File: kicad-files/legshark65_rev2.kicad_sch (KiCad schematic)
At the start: 203 parts, among them J1 ARM JTAG, SW1 K2-1187SQ-A4SW-06, SW2 PCM12SMTR, T2 53261-0471, U1 STM32F411CEU6, U2 MCP1700T-3302E/TT, U3 AT24C256C-SSHL-T, Y1 TAXM8M4RFDCET2T

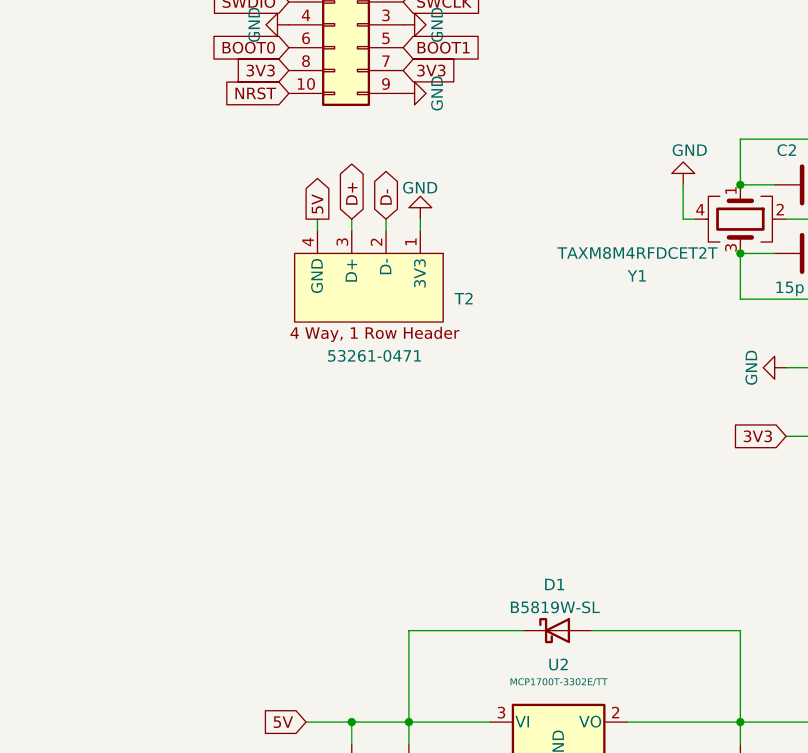
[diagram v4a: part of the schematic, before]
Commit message: Added EZMate connector and optional JST pads
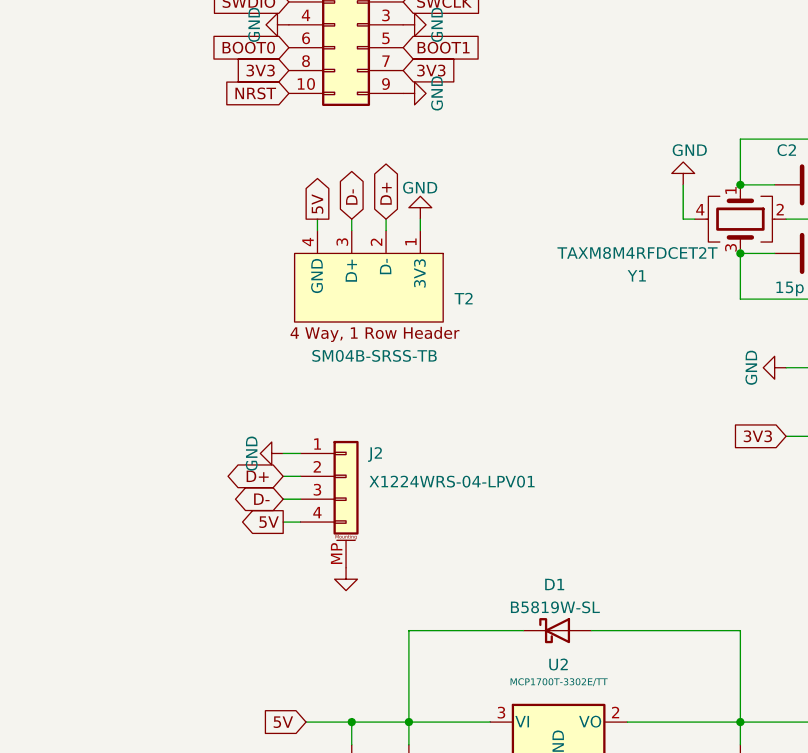
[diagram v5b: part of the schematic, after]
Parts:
- added J2: X1224WRS-04-LPV01, Legshark:PicoEZMate-Reinforced-Alt, symbol Connector_Generic_MountingPin:Conn_01x04_MountingPin
- T2: value 53261-0471 -> SM04B-SRSS-TB; footprint Legshark:Molex, PicoBlade, 53261, 4 Way, 1 Row, Right Angle PCB Header -> acheron_Connectors:SM04B-SRSS-TB(LF)(SN)
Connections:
- net 5V: now also J2.4 (Pin_4)
- net D+: now also T2.2 (D-), J2.2 (Pin_2); no longer T2.3 (D+)
- net D-: now also T2.3 (D+), J2.3 (Pin_3); no longer T2.2 (D-)
- net GND: now also J2.1 (Pin_1), J2.MP (MountPin)
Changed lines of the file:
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@@
     (stroke (width 0) (type default))
   )
+  (wire (pts (xy 41.91 266.065) (xy 43.815 266.065))
+    (stroke (width 0) (type default))
+  )
   (wire (pts (xy 325.12 16.51) (xy 325.12 24.13))
     (stroke (width 0) (type default))
@@
     (stroke (width 0) (type default))
   )
+  (wire (pts (xy 41.91 258.445) (xy 43.815 258.445))
+    (stroke (width 0) (type default))
+  )
   (wire (pts (xy 119.38 248.92) (xy 125.73 248.92))
     (stroke (width 0) (type default))
@@
     (stroke (width 0) (type default))
   )
+  (wire (pts (xy 43.815 260.985) (xy 41.91 260.985))
+    (stroke (width 0) (type default))
+  )
   (wire (pts (xy 91.44 158.75) (xy 96.52 158.75))
     (stroke (width 0) (type default))
@@
     (stroke (width 0) (type default))
   )
+  (wire (pts (xy 41.91 263.525) (xy 43.815 263.525))
+    (stroke (width 0) (type default))
+  )
   (wire (pts (xy 238.125 123.19) (xy 242.57 123.19))
     (stroke (width 0) (type default))
@@
     )
   )
-  (global_label "D-" (shape bidirectional) (at 53.34 232.41 90) (fields_autoplaced)
+  (global_label "5V" (shape output) (at 41.91 266.065 180) (fields_autoplaced)
+    (effects (font (size 1.27 1.27)) (justify right))
+    (property "Intersheetrefs" "${INTERSHEET_REFS}" (at 37.3603 266.065 0)
+      (effects (font (size 1.27 1.27)) (justify right) hide)
+    )
+  )
+  (global_label "D-" (shape bidirectional) (at 49.53 232.41 90) (fields_autoplaced)
     (effects (font (size 1.27 1.27)) (justify left))
-    (property "Intersheetrefs" "${INTERSHEET_REFS}" (at 53.34 226.3635 90)
+    (property "Intersheetrefs" "${INTERSHEET_REFS}" (at 49.53 226.3635 90)
       (effects (font (size 1.27 1.27)) (justify left) hide)
     )
@@
     )
   )
+  (global_label "D-" (shape bidirectional) (at 41.91 263.525 180) (fields_autoplaced)
+    (effects (font (size 1.27 1.27)) (justify right))
+    (property "Intersheetrefs" "${INTERSHEET_REFS}" (at 35.8635 263.525 0)
+      (effects (font (size 1.27 1.27)) (justify right) hide)
+    )
+  )
   (global_label "3V3" (shape input) (at 125.73 201.295 90) (fields_autoplaced)
     (effects (font (size 1.27 1.27)) (justify left))
@@
     )
   )
+  (global_label "D+" (shape bidirectional) (at 41.91 260.985 180) (fields_autoplaced)
+    (effects (font (size 1.27 1.27)) (justify right))
+    (property "Intersheetrefs" "${INTERSHEET_REFS}" (at 35.8635 260.985 0)
+      (effects (font (size 1.27 1.27)) (justify right) hide)
+    )
+  )
   (global_label "row4" (shape input) (at 125.73 223.52 180)
     (effects (font (size 1.27 1.27)) (justify right))
@@
     )
   )
-  (global_label "D+" (shape bidirectional) (at 49.53 232.41 90) (fields_autoplaced)
+  (global_label "D+" (shape bidirectional) (at 53.34 232.41 90) (fields_autoplaced)
     (effects (font (size 1.27 1.27)) (justify left))
-    (property "Intersheetrefs" "${INTERSHEET_REFS}" (at 49.53 226.3635 90)
+    (property "Intersheetrefs" "${INTERSHEET_REFS}" (at 53.34 226.3635 90)
       (effects (font (size 1.27 1.27)) (justify left) hide)
     )
@@
     )
   )
+  (symbol (lib_id "Connector_Generic_MountingPin:Conn_01x04_MountingPin") (at 48.895 260.985 0) (unit 1)
+    (in_bom yes) (on_board yes) (dnp no)
+    (property "Reference" "J2" (at 51.435 258.445 0)
+      (effects (font (size 1.27 1.27)) (justify left))
+    )
+    (property "Value" "X1224WRS-04-LPV01" (at 51.435 261.62 0)
+      (effects (font (size 1.27 1.27)) (justify left))
+    )
+    (property "Footprint" "Legshark:PicoEZMate-Reinforced-Alt" (at 48.895 260.985 0)
+      (effects (font (size 1.27 1.27)) hide)
+    )
+    (property "Datasheet" "~" (at 48.895 260.985 0)
+      (effects (font (size 1.27 1.27)) hide)
+    )
+    (property "Manufacturer" "XKB Connectivity" (at 48.895 260.985 0)
+      (effects (font (size 1.27 1.27)) hide)
+    )
+    (property "Manufacturer Part Number" "X1224WRS-04-LPV01" (at 48.895 260.985 0)
+      (effects (font (size 1.27 1.27)) hide)
+    )
+    (property "LCSC Part Number" "C528030" (at 48.895 260.985 0)
+      (effects (font (size 1.27 1.27)) hide)
+    )
+    (pin "1")
+    (pin "2")
+    (pin "3")
+    (pin "4")
+    (pin "MP")
+    (instances
+      (project "legshark65_rev2"
+        (path "/2fcc1073-d3f4-43f9-b3b4-5cee13272705"
+          (reference "J2") (unit 1)
+        )
+      )
+      (project "UDB"
+        (path "/c4c12ac1-bf97-4e49-b99b-b461a52b064e"
+          (reference "J2") (unit 1)
+        )
+      )
+    )
+  )
   (symbol (lib_id "Mechanical:MountingHole") (at 243.84 174.625 0) (unit 1)
     (in_bom yes) (on_board yes) (dnp no) (fields_autoplaced)
@@
     )
   )
+  (symbol (lib_id "power:GND") (at 48.895 271.145 0) (unit 1)
+    (in_bom yes) (on_board yes) (dnp no)
+    (property "Reference" "#PWR037" (at 48.895 277.495 0)
+      (effects (font (size 1.27 1.27)) hide)
+    )
+    (property "Value" "GND" (at 49.022 275.5392 0)
+      (effects (font (size 1.27 1.27)) hide)
+    )
+    (property "Footprint" "" (at 48.895 271.145 0)
+      (effects (font (size 1.27 1.27)) hide)
+    )
+    (property "Datasheet" "" (at 48.895 271.145 0)
+      (effects (font (size 1.27 1.27)) hide)
+    )
+    (pin "1")
+    (instances
+      (project "legshark65_rev2"
+        (path "/2fcc1073-d3f4-43f9-b3b4-5cee13272705"
+          (reference "#PWR037") (unit 1)
+        )
+      )
+      (project "UDB"
+        (path "/c4c12ac1-bf97-4e49-b99b-b461a52b064e"
+          (reference "#PWR011") (unit 1)
+        )
+      )
+    )
+  )
   (symbol (lib_id "Device:R") (at 179.07 289.56 180) (unit 1)
     (in_bom yes) (on_board yes) (dnp no)
@@
       (effects (font (size 1.27 1.27)) (justify left))
     )
-    (property "Value" "53261-0471" (at 52.07 247.65 90)
+    (property "Value" "SM04B-SRSS-TB" (at 52.07 247.65 90)
       (effects (font (size 1.27 1.27)))
     )
-    (property "Footprint" "Legshark:Molex, PicoBlade, 53261, 4 Way, 1 Row, Right Angle PCB Header" (at 40.64 238.76 0)
+    (property "Footprint" "acheron_Connectors:SM04B-SRSS-TB(LF)(SN)" (at 40.64 238.76 0)
       (effects (font (size 1.27 1.27)) hide)
     )
-    (property "Datasheet" "https://docs.rs-online.com/4dcc/0900766b8150e34b.pdf" (at 64.77 241.3 0)
+    (property "Datasheet" "https://www.digikey.com.au/en/products/detail/jst-sales-america-inc/SM04B-SRSS-TB-LF-SN/926710" (at 64.77 241.3 0)
       (effects (font (size 1.27 1.27)) hide)
     )
@@
         )
       )
+    )
+  )
+  (symbol (lib_id "power:GND") (at 41.91 258.445 270) (unit 1)
+    (in_bom yes) (on_board yes) (dnp no)
+    (property "Reference" "#PWR038" (at 35.56 258.445 0)
+      (effects (font (size 1.27 1.27)) hide)
+    )
+    (property "Value" "GND" (at 38.4603 260.4596 0)
+      (effects (font (size 1.27 1.27)) (justify right))
+    )
+    (property "Footprint" "" (at 41.91 258.445 0)
+      (effects (font (size 1.27 1.27)) hide)
+    )
+    (property "Datasheet" "" (at 41.91 258.445 0)
+      (effects (font (size 1.27 1.27)) hide)
+    )
+    (pin "1")
+    (instances
+      (project "legshark65_rev2"
+        (path "/2fcc1073-d3f4-43f9-b3b4-5cee13272705"
+          (reference "#PWR038") (unit 1)
+        )
+      )
+      (project "old_layout"
+        (path "/2fda2561-53ed-4930-8b41-858e0e3dd5f4"
+          (reference "#PWR031") (unit 1)
+        )
+      )
+      (project "legshark65_rev1"
+        (path "/9ddf6dc5-8b5e-413a-9b25-d1d5a5a60469"
+          (reference "#PWR02") (unit 1)
+        )
+      )

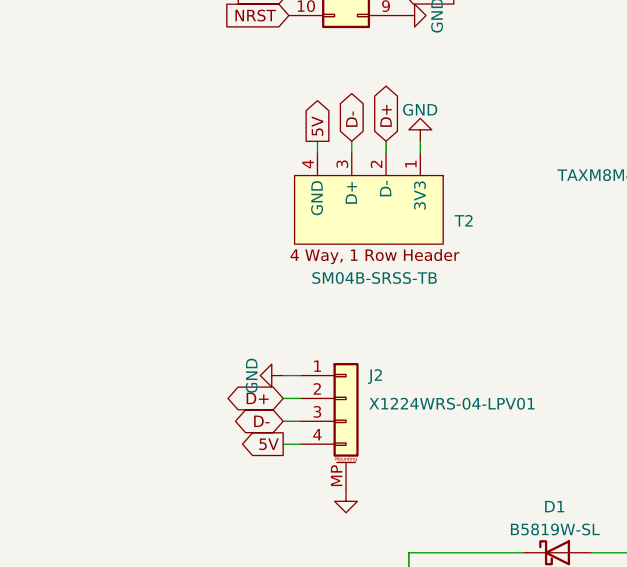
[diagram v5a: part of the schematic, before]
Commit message: Added wired option and some minor changes
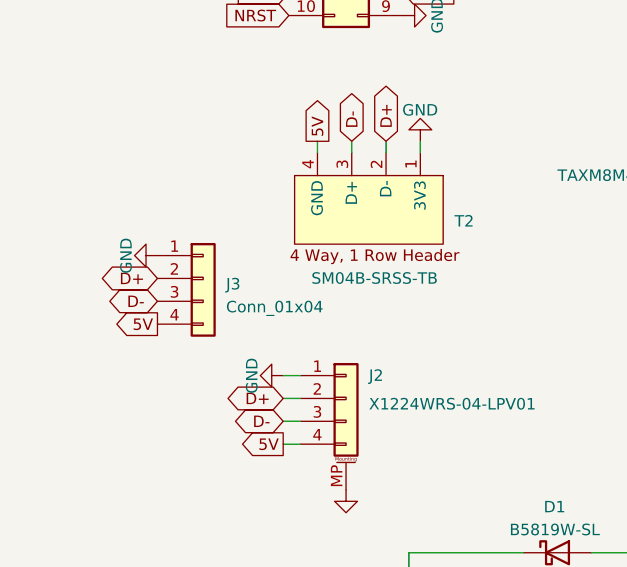
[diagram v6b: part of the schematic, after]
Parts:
- added J3: Conn_01x04, acheron_Connectors:PinHeader_1x4_P2.54mm_Vertical, symbol Connector_Generic:Conn_01x04
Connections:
- net 5V: now also J3.4 (Pin_4)
- net D+: now also J3.2 (Pin_2)
- net D-: now also J3.3 (Pin_3)
- net GND: now also J3.1 (Pin_1)
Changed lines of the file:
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@@
     )
   )
+  (global_label "5V" (shape output) (at 27.94 252.73 180) (fields_autoplaced)
+    (effects (font (size 1.27 1.27)) (justify right))
+    (property "Intersheetrefs" "${INTERSHEET_REFS}" (at 23.3903 252.73 0)
+      (effects (font (size 1.27 1.27)) (justify right) hide)
+    )
+  )
   (global_label "row4" (shape input) (at 125.73 223.52 180)
     (effects (font (size 1.27 1.27)) (justify right))
@@
     )
   )
+  (global_label "D+" (shape bidirectional) (at 27.94 247.65 180) (fields_autoplaced)
+    (effects (font (size 1.27 1.27)) (justify right))
+    (property "Intersheetrefs" "${INTERSHEET_REFS}" (at 21.8935 247.65 0)
+      (effects (font (size 1.27 1.27)) (justify right) hide)
+    )
+  )
   (global_label "3V3" (shape input) (at 134.62 182.88 90) (fields_autoplaced)
     (effects (font (size 1.27 1.27)) (justify left))
@@
     )
   )
+  (global_label "D-" (shape bidirectional) (at 27.94 250.19 180) (fields_autoplaced)
+    (effects (font (size 1.27 1.27)) (justify right))
+    (property "Intersheetrefs" "${INTERSHEET_REFS}" (at 21.8935 250.19 0)
+      (effects (font (size 1.27 1.27)) (justify right) hide)
+    )
+  )
   (global_label "row2" (shape input) (at 213.36 262.89 0)
     (effects (font (size 1.27 1.27)) (justify left))
@@
     )
   )
+  (symbol (lib_id "power:GND") (at 27.94 245.11 270) (unit 1)
+    (in_bom yes) (on_board yes) (dnp no)
+    (property "Reference" "#PWR035" (at 21.59 245.11 0)
+      (effects (font (size 1.27 1.27)) hide)
+    )
+    (property "Value" "GND" (at 24.4903 247.1246 0)
+      (effects (font (size 1.27 1.27)) (justify right))
+    )
+    (property "Footprint" "" (at 27.94 245.11 0)
+      (effects (font (size 1.27 1.27)) hide)
+    )
+    (property "Datasheet" "" (at 27.94 245.11 0)
+      (effects (font (size 1.27 1.27)) hide)
+    )
+    (pin "1")
+    (instances
+      (project "legshark65_rev2"
+        (path "/2fcc1073-d3f4-43f9-b3b4-5cee13272705"
+          (reference "#PWR035") (unit 1)
+        )
+      )
+      (project "old_layout"
+        (path "/2fda2561-53ed-4930-8b41-858e0e3dd5f4"
+          (reference "#PWR031") (unit 1)
+        )
+      )
+      (project "legshark65_rev1"
+        (path "/9ddf6dc5-8b5e-413a-9b25-d1d5a5a60469"
+          (reference "#PWR02") (unit 1)
+        )
+      )
+    )
+  )
   (symbol (lib_id "power:GND") (at 55.245 218.44 90) (unit 1)
     (in_bom yes) (on_board yes) (dnp no)
@@
         )
       )
+    )
+  )
+  (symbol (lib_id "Connector_Generic:Conn_01x04") (at 33.02 247.65 0) (unit 1)
+    (in_bom yes) (on_board yes) (dnp no) (fields_autoplaced)
+    (property "Reference" "J3" (at 35.56 248.285 0)
+      (effects (font (size 1.27 1.27)) (justify left))
+    )
+    (property "Value" "Conn_01x04" (at 35.56 250.825 0)
+      (effects (font (size 1.27 1.27)) (justify left))
+    )
+    (property "Footprint" "acheron_Connectors:PinHeader_1x4_P2.54mm_Vertical" (at 33.02 247.65 0)
+      (effects (font (size 1.27 1.27)) hide)
+    )
+    (property "Datasheet" "~" (at 33.02 247.65 0)
+      (effects (font (size 1.27 1.27)) hide)
+    )
+    (pin "1")
+    (pin "2")
+    (pin "3")
+    (pin "4")
+    (instances
+      (project "legshark65_rev2"
+        (path "/2fcc1073-d3f4-43f9-b3b4-5cee13272705"
+          (reference "J3") (unit 1)
+        )
+      )
+      (project "legshark65_rev1"
+        (path "/9ddf6dc5-8b5e-413a-9b25-d1d5a5a60469"
+          (reference "J2") (unit 1)
+        )
+      )

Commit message: Finally happy with the graphics
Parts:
- added H2: OSH, acheron_Graphics:OSH_Logo_22.5x8.5mm, symbol Mechanical:MountingHole
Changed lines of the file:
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@@
+    )
+  )
+  (symbol (lib_id "Mechanical:MountingHole") (at 243.84 187.325 0) (unit 1)
+    (in_bom yes) (on_board yes) (dnp no) (fields_autoplaced)
+    (property "Reference" "H2" (at 247.015 186.69 0)
+      (effects (font (size 1.27 1.27)) (justify left))
+    )
+    (property "Value" "OSH" (at 247.015 189.23 0)
+      (effects (font (size 1.27 1.27)) (justify left))
+    )
+    (property "Footprint" "acheron_Graphics:OSH_Logo_22.5x8.5mm" (at 243.84 187.325 0)
+      (effects (font (size 1.27 1.27)) hide)
+    )
+    (property "Datasheet" "~" (at 243.84 187.325 0)
+      (effects (font (size 1.27 1.27)) hide)
+    )
+    (instances
+      (project "legshark65_rev2"
+        (path "/2fcc1073-d3f4-43f9-b3b4-5cee13272705"
+          (reference "H2") (unit 1)
+        )
+      )
+      (project "legshark65_rev1"
+        (path "/9ddf6dc5-8b5e-413a-9b25-d1d5a5a60469"
+          (reference "H3") (unit 1)
+        )
+      )
     )
   )
